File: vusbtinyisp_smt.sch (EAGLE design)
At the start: 9 parts, among them J1 AVR_SPI_PRG_6NS, U1 Tiny85-20-SMT

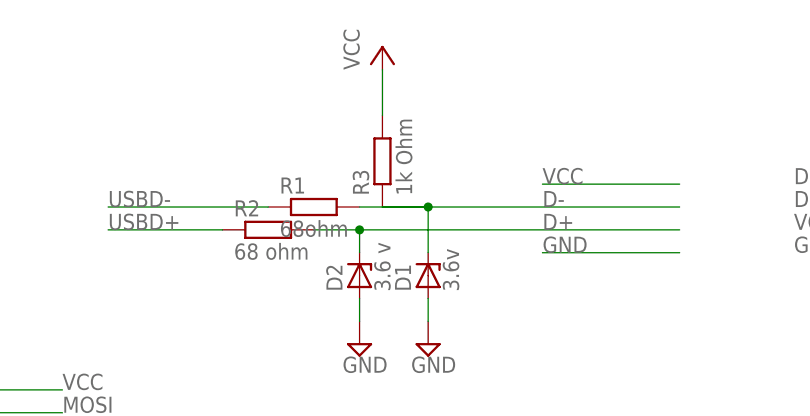
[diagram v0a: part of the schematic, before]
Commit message: changing 1k to 1.5k resistors in 5V designs
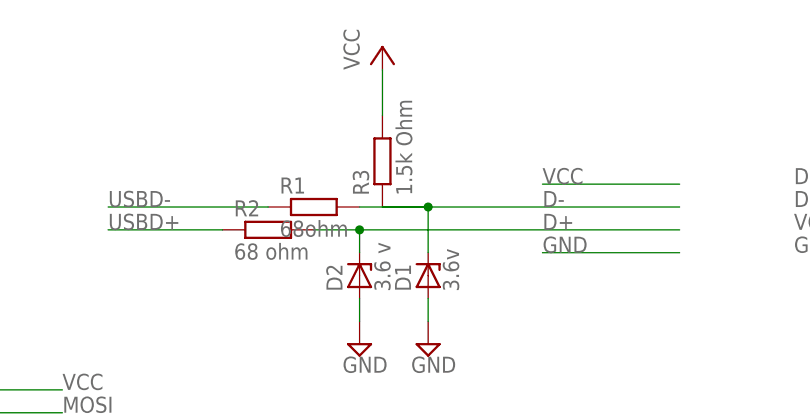
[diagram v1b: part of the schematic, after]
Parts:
- R3: value 1k Ohm -> 1.5k Ohm
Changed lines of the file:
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@@
 <part name="SUPPLY3" library="supply2" deviceset="GND" device=""/>
 <part name="P+2" library="supply1" deviceset="VCC" device=""/>
-<part name="R3" library="resistor" deviceset="R-EU_" device="R1206" value="1k Ohm"/>
+<part name="R3" library="resistor" deviceset="R-EU_" device="R1206" value="1.5k Ohm"/>
 <part name="J1" library="SparkFun-Connectors" deviceset="AVR_SPI_PRG_6" device="NS"/>
 <part name="JP2" library="SparkFun-Connectors" deviceset="USB" device="SMD"/>
